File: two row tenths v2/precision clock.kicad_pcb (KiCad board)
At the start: 2 copper layers, 157 x 53 mm, 59 parts, among them P1 USB_C_Plug_USB2.0, P2 USB_C_Plug_USB2.0, Q1 MMBT3904

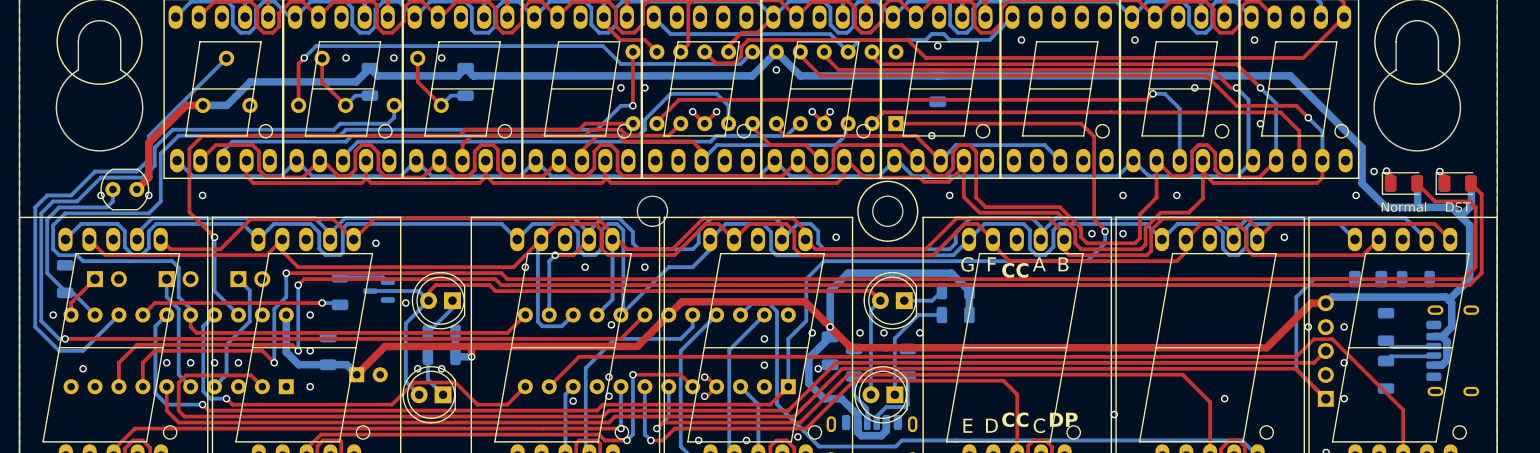
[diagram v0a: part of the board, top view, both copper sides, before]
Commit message: Add 74AHCT125 as PWM driver
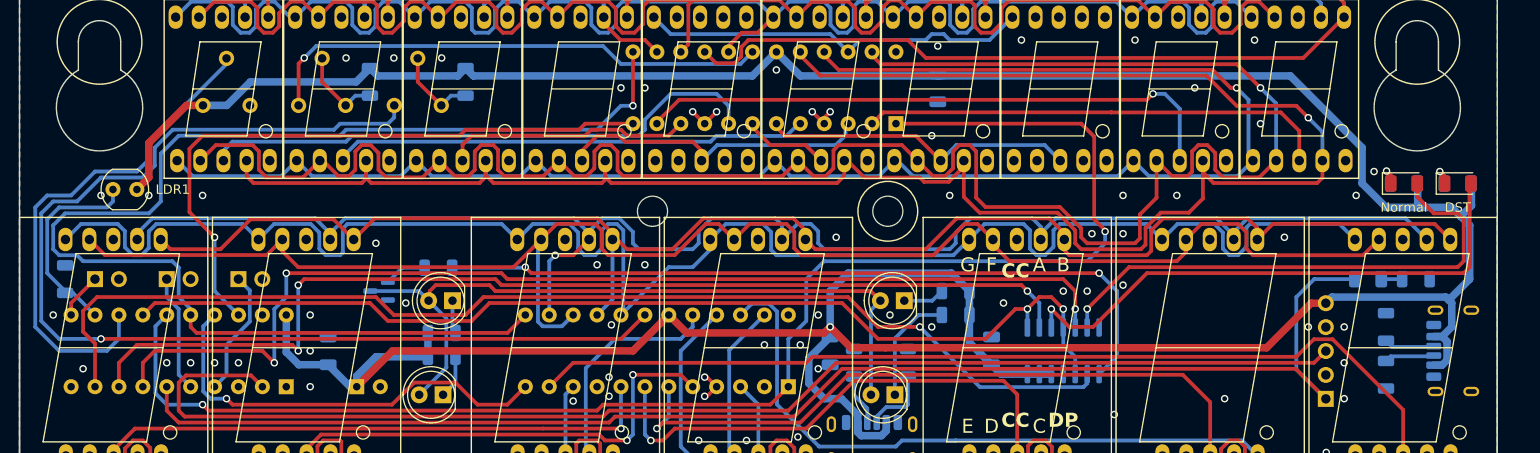
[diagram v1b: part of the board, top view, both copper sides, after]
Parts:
- added C5: 0.1uF, Capacitor_SMD:C_1206_3216Metric, B.Cu at (128.3, 100.3)
- added U1: 74AHCT125, Package_SO:SOIC-14_3.9x8.7mm_P1.27mm, B.Cu at (135.9, 100.3)
- C3: footprint Capacitor_THT:CP_Radial_D5.0mm_P2.50mm -> Capacitor_THT:CP_Radial_D6.3mm_P2.50mm
- moved R6 10.7 mm to (69.5, 91.5), turned to 180 degrees
- moved C3 1.27 mm to (60.8, 104.1)
- turned R1 to 180 degrees
- turned R3 to 180 degrees
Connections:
- D_BST1 pad 2: BST -> Net-(D_BST1-A)
- D_GMT1 pad 2: GMT -> Net-(D_GMT1-A)
- R6 pad 1: ColonPWM -> Net-(R6-Pad1)
- U_CONTROL1 pad 14: ColonPWM -> PWM
- U_CONTROL1 pad 9: unconnected-(U_CONTROL1-(PCINT16/OC0B/T1)PD5-Pad9) -> COLON
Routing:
- net COLON: track 0.00 -> 122.5 mm, vias 0 -> 1
- net PWM: track 0.00 -> 113.3 mm, vias 0 -> 2
- net Net-(R6-Pad1): track 0.00 -> 81.3 mm, vias 0 -> 2
- net Net-(D_BST1-A): track 0.00 -> 58.8 mm, vias 0 -> 1
- net Net-(D_GMT1-A): track 0.00 -> 55.9 mm, vias 0 -> 1
- net BST: track 166.6 -> 112.3 mm, vias 2 -> 3
- net GMT: track 168.4 -> 116.1 mm, vias 2 -> 3
- net ColonPWM: track 21.6 -> 0.00 mm, vias 1 -> 0
- net +5V: track 370.8 -> 391.0 mm, vias 2 -> 1
- net LightSet: track 52.6 -> 54.1 mm
- net Net-(DColonHM2-K): track 4.51 -> 3.55 mm
- net Net-(Q1-B): track 5.29 -> 4.54 mm

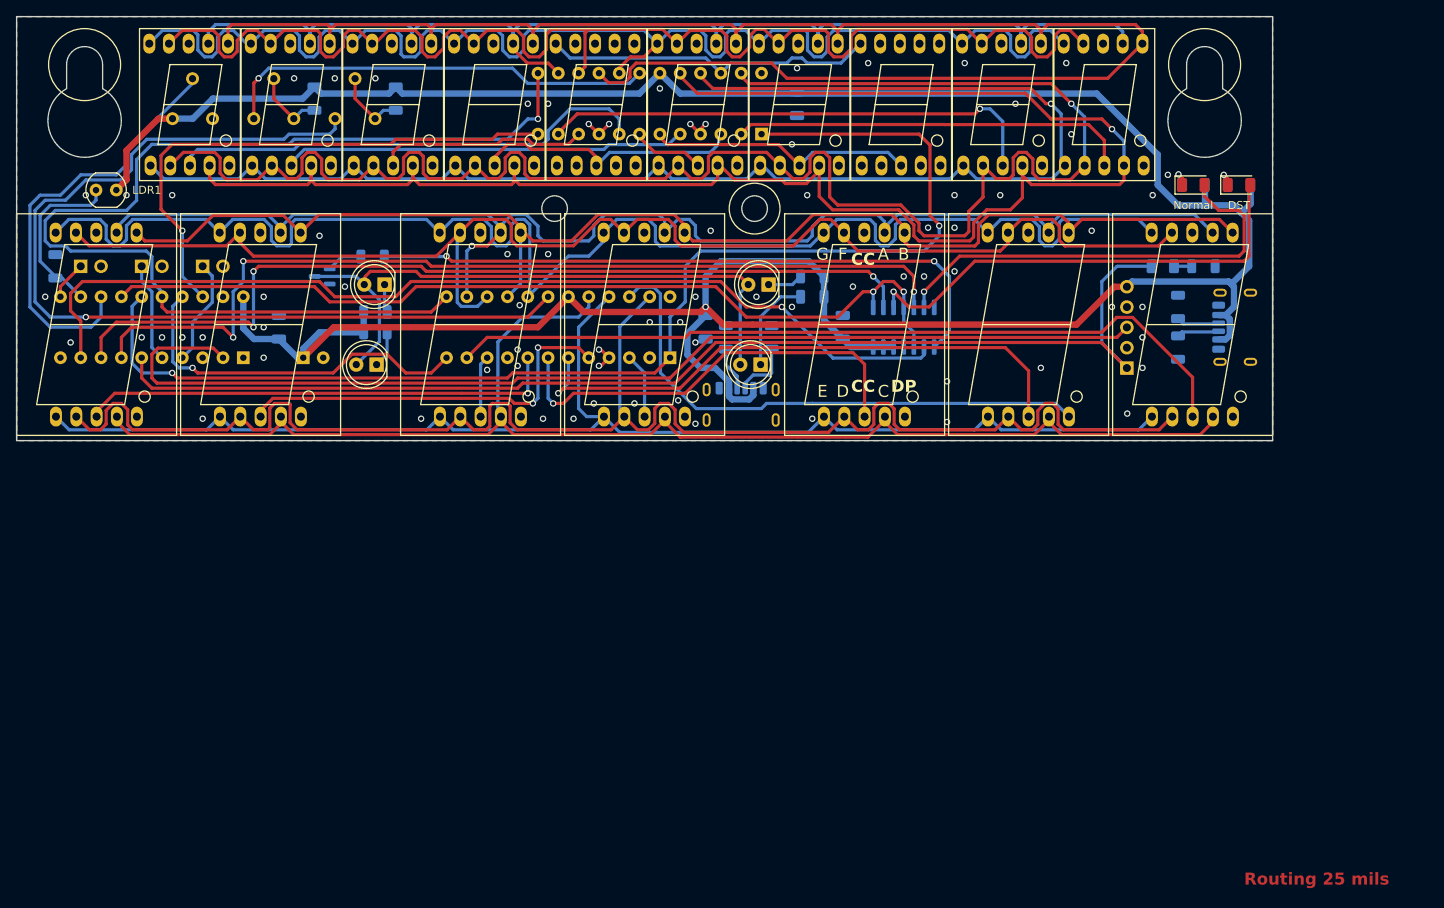
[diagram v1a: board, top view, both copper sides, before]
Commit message: Add optional crystal
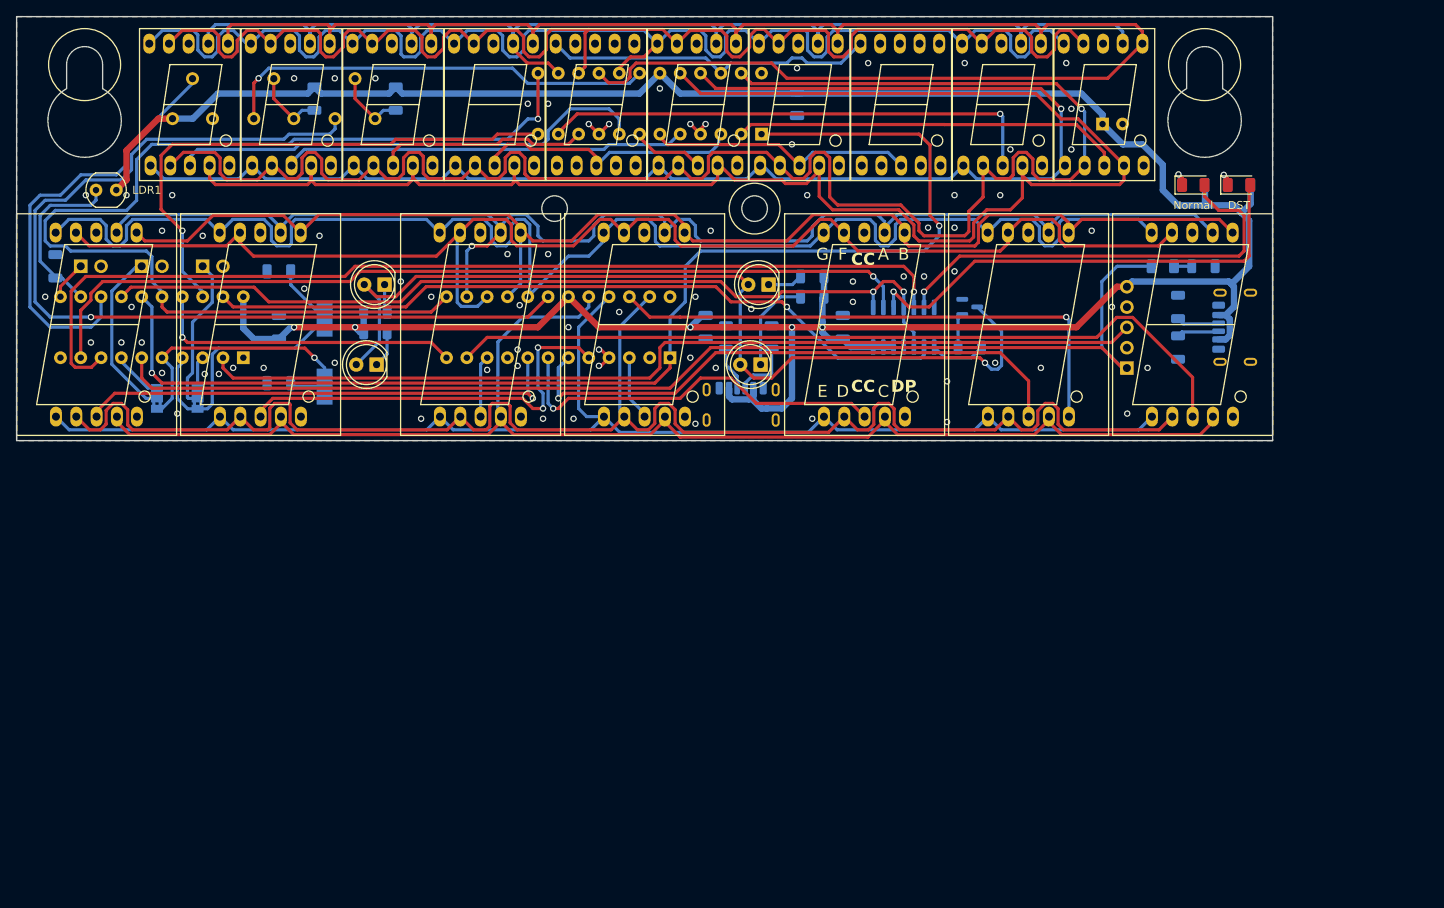
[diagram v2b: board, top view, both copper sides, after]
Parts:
- added C6: 22pF, Capacitor_SMD:C_1206_3216Metric, B.Cu at (57.8, 93.3)
- added C7: 22pF, Capacitor_SMD:C_1206_3216Metric, B.Cu at (57.8, 107.3)
- added JP4: Jumper_3_Bridged12, Jumper:SolderJumper-3_P1.3mm_Bridged2Bar12_Pad1.0x1.5mm, B.Cu at (47.6, 109.2)
- added JP5: Jumper_3_Bridged12, Jumper:SolderJumper-3_P1.3mm_Bridged2Bar12_Pad1.0x1.5mm, B.Cu at (42.5, 109.2)
- added Y1: Crystal, Crystal:Crystal_SMD_HC49-SD, B.Cu at (63.5, 103.5)
- moved C3 104.1 mm to (160.7, 74.9)
- moved Q1 81.0 mm to (144.1, 97.8), turned to 0 degrees
- moved R6 75.5 mm to (144.1, 102.9)
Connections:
- JP1 pad 1: /UTC* -> Net-(JP1-A)
- JP2 pad 1: /PERM_DST* -> Net-(JP2-A)
- U_CONTROL1 pad 19: unconnected-(U_CONTROL1-(PCINT7/USCK/SCK/SCL)PB7-Pad19) -> COLON
- U_CONTROL1 pad 3: unconnected-(U_CONTROL1-(PCINT12/TXD)PD1-Pad3) -> UTC_XTAL
- U_CONTROL1 pad 4: /UTC* -> UTC
- U_CONTROL1 pad 5: /PERM_DST* -> PermDST
- U_CONTROL1 pad 7: GMT -> PermDST_XTAL
- U_CONTROL1 pad 8: BST -> GMT
- U_CONTROL1 pad 9: COLON -> BST
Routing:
- net Net-(R6-Pad1): track 81.3 -> 6.99 mm, vias 2 -> 0
- net UTC: track 0.00 -> 40.3 mm
- net Net-(DColonHM1-A): track 78.9 -> 116.3 mm, vias 0 -> 1
- net PermDST: track 0.00 -> 37.0 mm, vias 0 -> 1
- net COLON: track 122.5 -> 94.1 mm
- net +5V: track 391.0 -> 366.1 mm, vias 1 -> 5
- net Net-(JP2-A): track 0.00 -> 21.6 mm
- net Net-(JP1-A): track 0.00 -> 19.5 mm
- net /GPS_DATA: track 137.7 -> 118.9 mm
- net /UTC*: track 13.5 -> 0.00 mm
- net /PERM_DST*: track 12.5 -> 0.00 mm
- net GMT: track 116.1 -> 124.5 mm, vias 3 -> 1
- net LD_TIME: track 46.1 -> 39.2 mm
- net PermDST_XTAL: track 0.00 -> 6.29 mm
- net Net-(UTimeDrv1-DIG_3): track 54.7 -> 49.1 mm
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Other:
- board text added: "Antenna mount"
- board text added: "External Crystal 8 MHz"
- board text added: "Int RC"
- board text added: "XTAL"
- board text removed: "Ant. mount"
- board text removed: "Routing 25 mils"

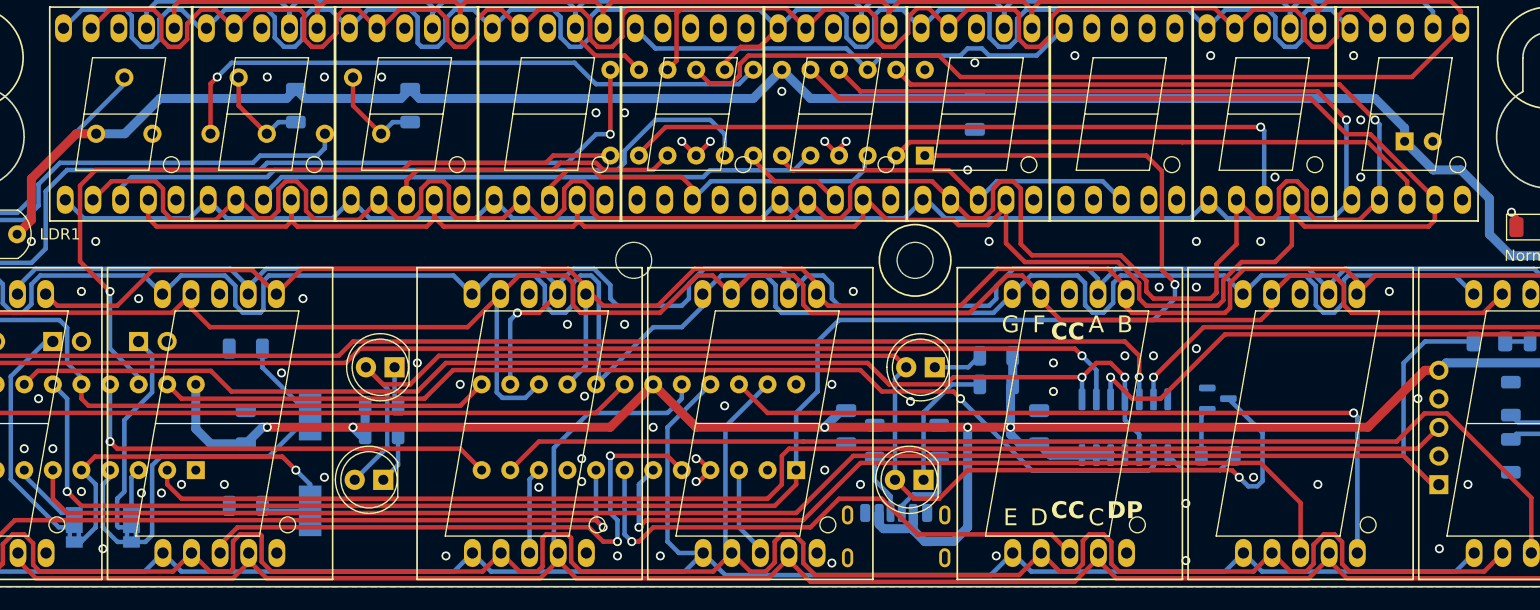
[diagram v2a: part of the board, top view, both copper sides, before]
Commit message: Add GPS model, sending to production.
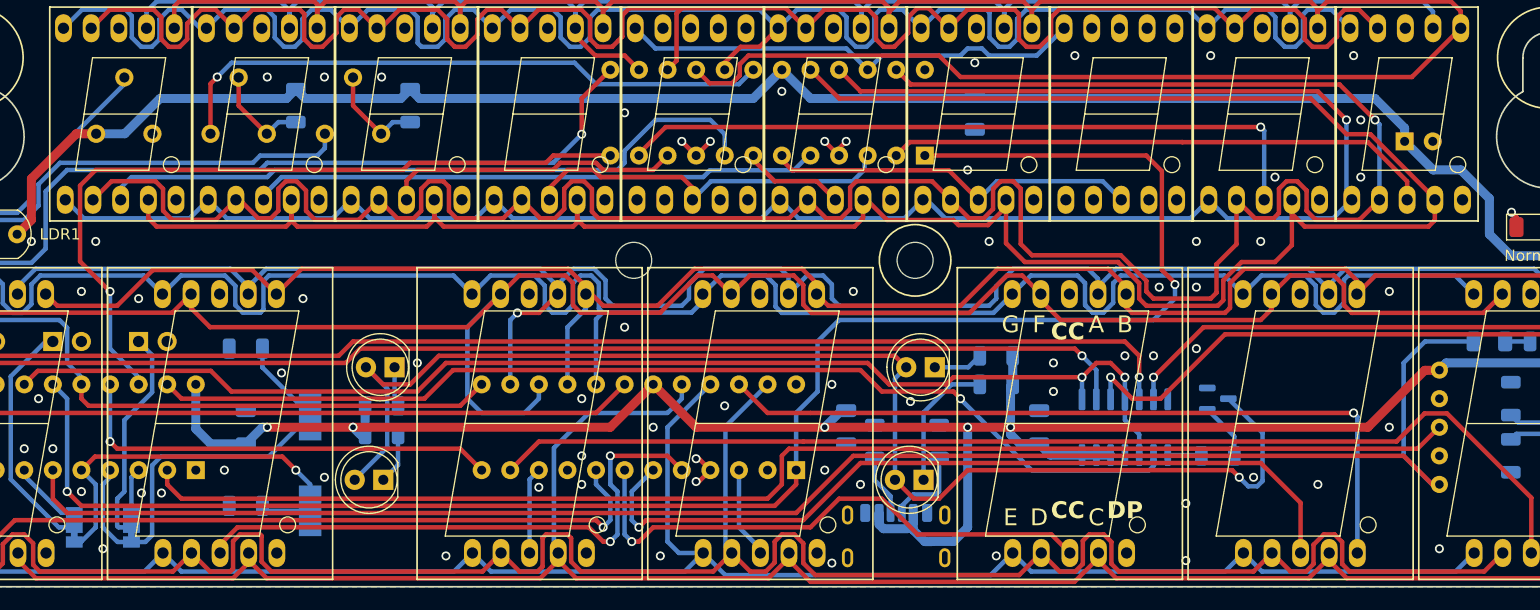
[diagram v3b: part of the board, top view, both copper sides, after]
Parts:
- JP4, JP5: footprint Jumper:SolderJumper-3_P1.3mm_Bridged2Bar12_Pad1.0x1.5mm -> Jumper:SolderJumper-3_P1.3mm_Bridged12_Pad1.0x1.5mm
- R15: value 20K -> 10K
- U_GPS1: footprint Connector_PinSocket_2.54mm:PinSocket_1x05_P2.54mm_Horizontal -> precision clock:ublox_GPS
- moved U_GPS1 20.9 mm to (143.5, 100.3)
- turned R6 to 0 degrees
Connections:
- net PermDST renamed PermDST_NO_XTAL
- net UTC renamed UTC_NO_XTAL
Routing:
- net /timeF: track 172.0 -> 177.9 mm
- net Net-(R6-Pad1): track 6.99 -> 3.01 mm
- net /timeG: track 185.3 -> 182.1 mm
- net SPI_CLK: track 135.7 -> 134.2 mm
- net Net-(Q1-B): track 4.35 -> 5.12 mm
- net Net-(UTimeDrv1-DIG_7): track 61.7 -> 62.3 mm
- net Net-(UTimeDrv1-DIG_2): track 72.7 -> 73.2 mm
- net GND: vias 77 -> 71
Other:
- board text removed: "GND"
- board text removed: "PPS"
- board text removed: "RXD"
- board text removed: "TXD"
- board text removed: "VCC"

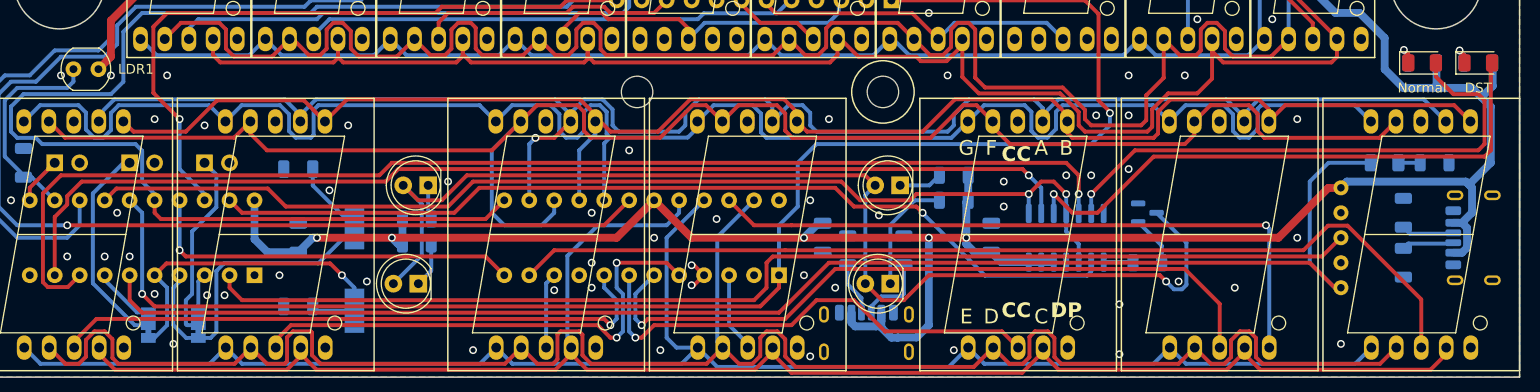
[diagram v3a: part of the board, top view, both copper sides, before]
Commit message: Fix LED polarity, add STLs for antenna mounts
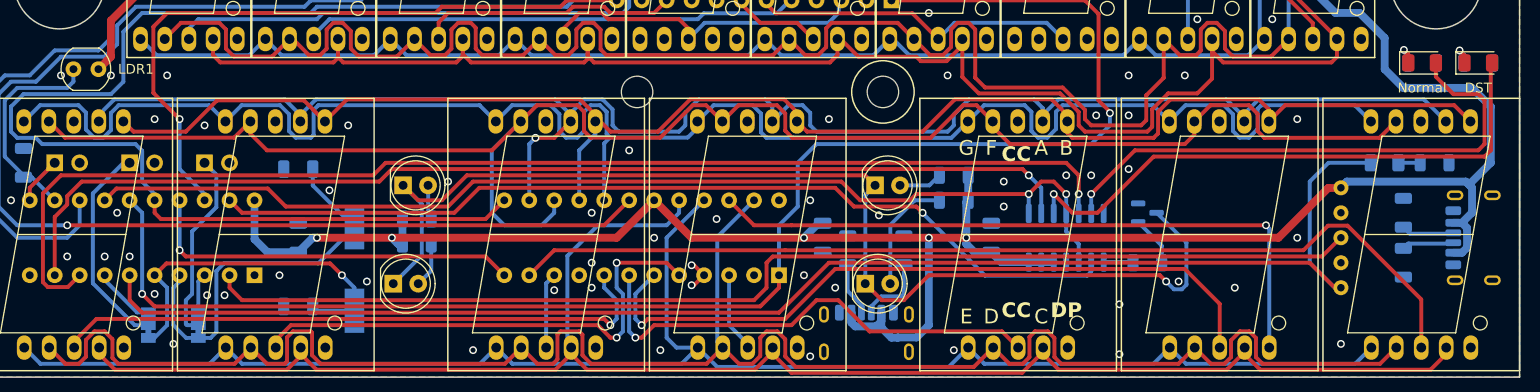
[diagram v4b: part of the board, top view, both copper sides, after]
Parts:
- R1, R3, R5, R7: value 330 -> 1k
- moved DColonHM1 2.55 mm to (67.5, 105.0), turned to 0 degrees
- moved DColonHM2 2.55 mm to (68.5, 95.0), turned to 0 degrees
- moved DColonMS1 2.55 mm to (115.5, 105.0), turned to 0 degrees
- moved DColonMS2 2.55 mm to (116.5, 95.0), turned to 0 degrees
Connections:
- DColonHM2 pad 1: Net-(DColonHM2-K) -> Net-(DColonHM1-K)
- DColonHM2 pad 2: Net-(DColonHM1-A) -> Net-(DColonHM2-A)
- DColonMS1 pad 1: Net-(DColonMS1-K) -> Net-(DColonHM1-K)
- DColonMS1 pad 2: Net-(DColonHM1-A) -> Net-(DColonMS1-A)
- DColonMS2 pad 1: Net-(DColonMS2-K) -> Net-(DColonHM1-K)
- DColonMS2 pad 2: Net-(DColonHM1-A) -> Net-(DColonMS2-A)
- Q1 pad 3: Net-(DColonHM1-A) -> Net-(DColonHM1-K)
- R1 pad 1: Net-(DColonHM1-K) -> Net-(DColonHM1-A)
- R2 pad 2: +5V -> GND
- R3 pad 1: Net-(DColonHM2-K) -> Net-(DColonHM2-A)
- R4 pad 2: +5V -> GND
- R5 pad 1: Net-(DColonMS1-K) -> Net-(DColonMS1-A)
- R7 pad 1: Net-(DColonMS2-K) -> Net-(DColonMS2-A)
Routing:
- net Net-(DColonHM1-K): track 4.58 -> 116.3 mm, vias 0 -> 1
- net Net-(DColonHM1-A): track 116.3 -> 4.58 mm, vias 1 -> 0
- net Net-(DColonMS1-K): track 12.0 -> 0.00 mm
- net Net-(DColonMS1-A): track 0.00 -> 12.0 mm
- net +5V: track 366.1 -> 359.5 mm
- net Net-(DColonMS2-K): track 4.42 -> 0.00 mm
- net Net-(DColonMS2-A): track 0.00 -> 4.42 mm
- net Net-(DColonHM2-K): track 3.55 -> 0.00 mm
- net Net-(DColonHM2-A): track 0.00 -> 3.55 mm
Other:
- board text added: "Two-row version 2.1 SolidElectronics 2025"
- board text removed: "Two-row version 2.0 SolidElectronics 2025"
